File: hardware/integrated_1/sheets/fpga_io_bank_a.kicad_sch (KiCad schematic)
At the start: 1 part, among them U1 XC6SLX9-TQG144

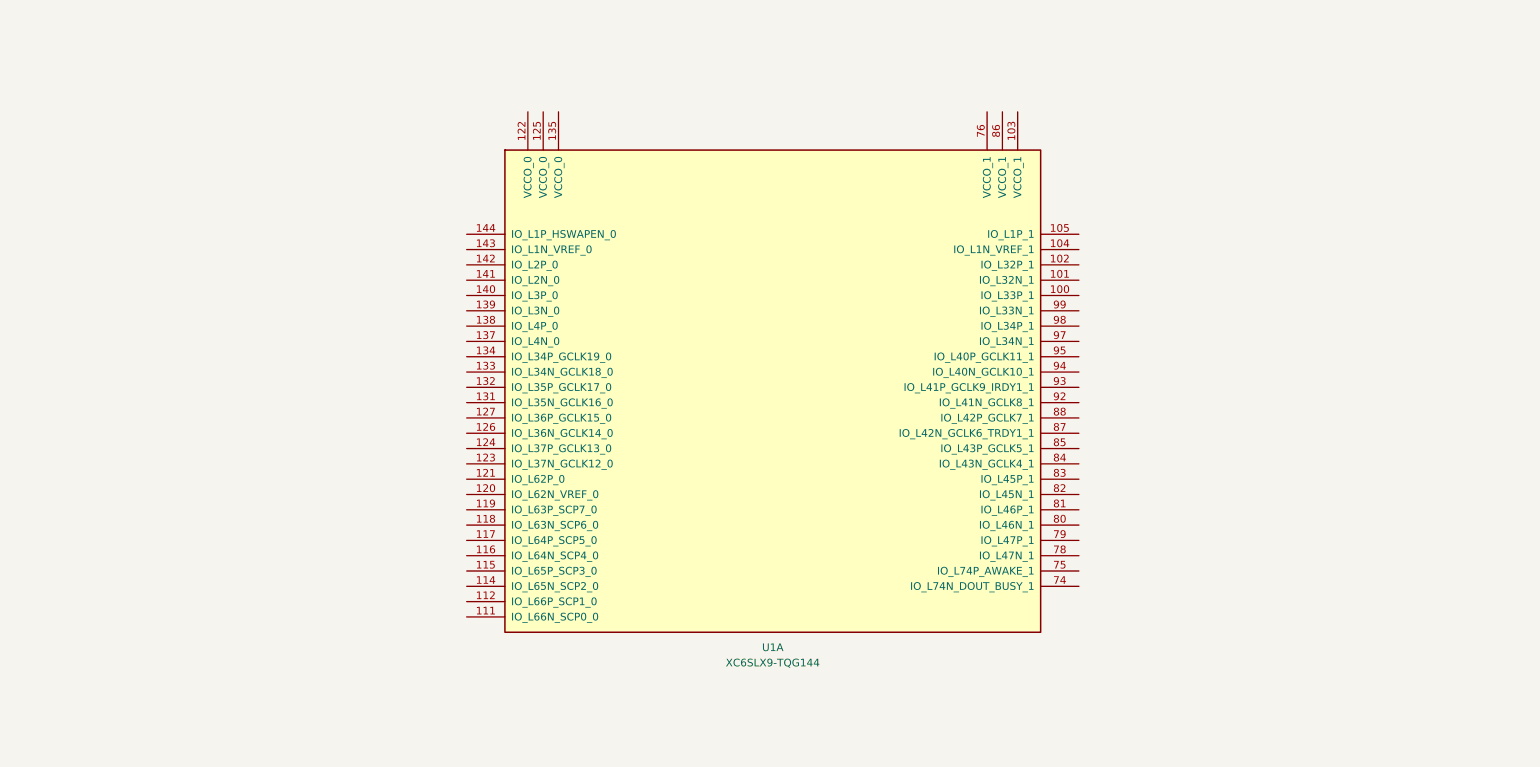
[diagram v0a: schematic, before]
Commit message: hooked up dvi and rp2040 to fpga
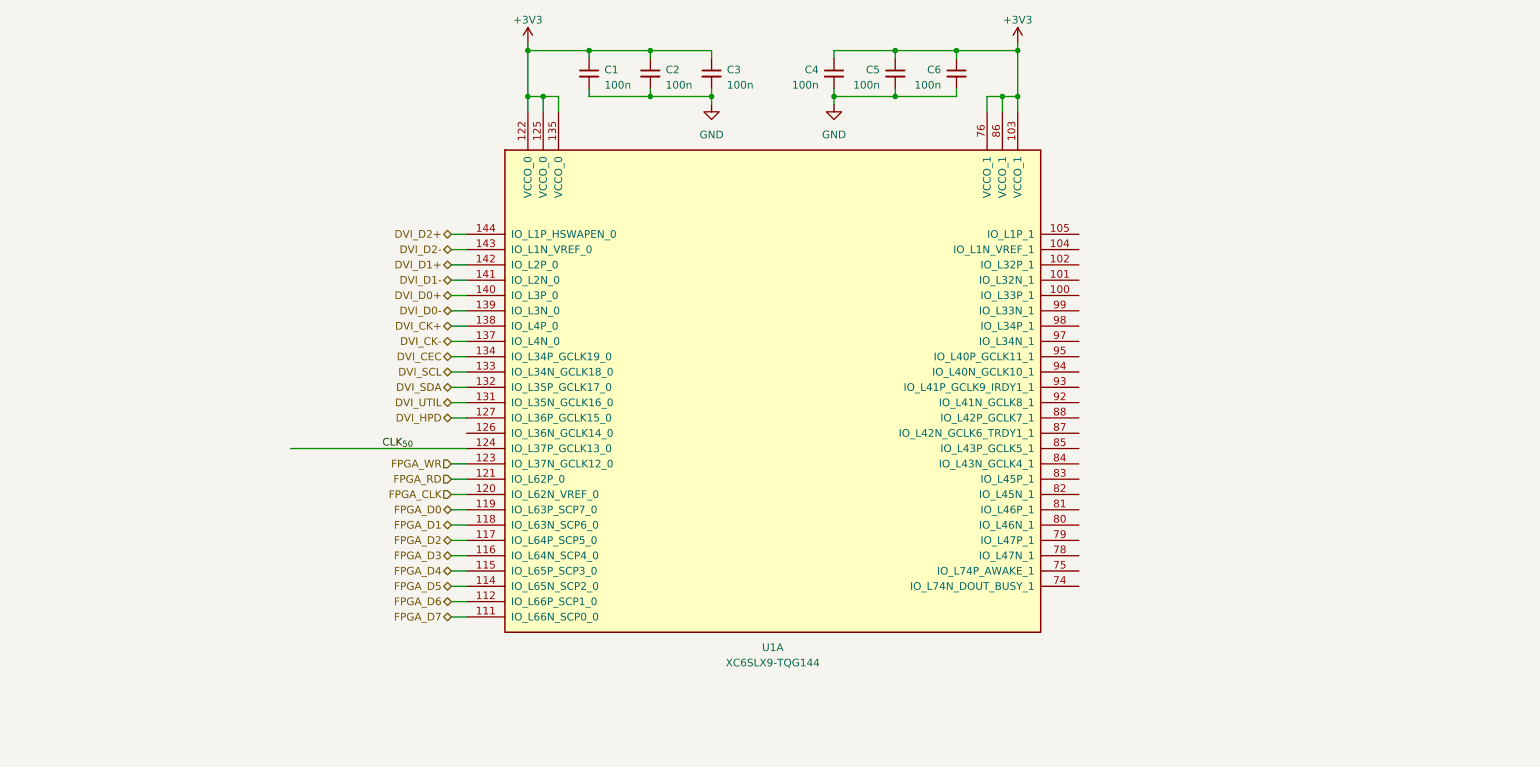
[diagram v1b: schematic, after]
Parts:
- added C1, C2, C3, C4, C5, C6: 100n, Capacitor_SMD:C_0402_1005Metric, symbol Device:C_Small
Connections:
- net +3V3: now reaches U1.103 (VCCO_1)
- net +3V3: now also U1.122 (VCCO_0), U1.125 (VCCO_0), U1.135 (VCCO_0), U1.76 (VCCO_1), U1.86 (VCCO_1), C1.1, C2.1, C3.1, C4.1, C5.1, C6.1
- net FPGA_D7: now reaches U1.111 (IO_L66N_SCP0_0)
- net FPGA_D6: now reaches U1.112 (IO_L66P_SCP1_0)
- net FPGA_D5: now reaches U1.114 (IO_L65N_SCP2_0)
- net FPGA_D4: now reaches U1.115 (IO_L65P_SCP3_0)
- net FPGA_D3: now reaches U1.116 (IO_L64N_SCP4_0)
- net FPGA_D2: now reaches U1.117 (IO_L64P_SCP5_0)
- net FPGA_D1: now reaches U1.118 (IO_L63N_SCP6_0)
- net FPGA_D0: now reaches U1.119 (IO_L63P_SCP7_0)
- net FPGA_CLK: now reaches U1.120 (IO_L62N_VREF_0)
- net FPGA_RD: now reaches U1.121 (IO_L62P_0)
- net FPGA_WR: now reaches U1.123 (IO_L37N_GCLK12_0)
- net CLK_{50}: now reaches U1.124 (IO_L37P_GCLK13_0)
- net DVI_HPD: now reaches U1.127 (IO_L36P_GCLK15_0)
- net DVI_UTIL: now reaches U1.131 (IO_L35N_GCLK16_0)
- net DVI_SDA: now reaches U1.132 (IO_L35P_GCLK17_0)
- net DVI_SCL: now reaches U1.133 (IO_L34N_GCLK18_0)
- net DVI_CEC: now reaches U1.134 (IO_L34P_GCLK19_0)
- net DVI_CK-: now reaches U1.137 (IO_L4N_0)
- net DVI_CK+: now reaches U1.138 (IO_L4P_0)
- net DVI_D0-: now reaches U1.139 (IO_L3N_0)
- net DVI_D0+: now reaches U1.140 (IO_L3P_0)
- net DVI_D1-: now reaches U1.141 (IO_L2N_0)
- net DVI_D1+: now reaches U1.142 (IO_L2P_0)
- net DVI_D2-: now reaches U1.143 (IO_L1N_VREF_0)
- net DVI_D2+: now reaches U1.144 (IO_L1P_HSWAPEN_0)
- new net GND: C1.2, C2.2, C3.2, C4.2, C5.2, C6.2

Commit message: rearranged the pinout to make more sense
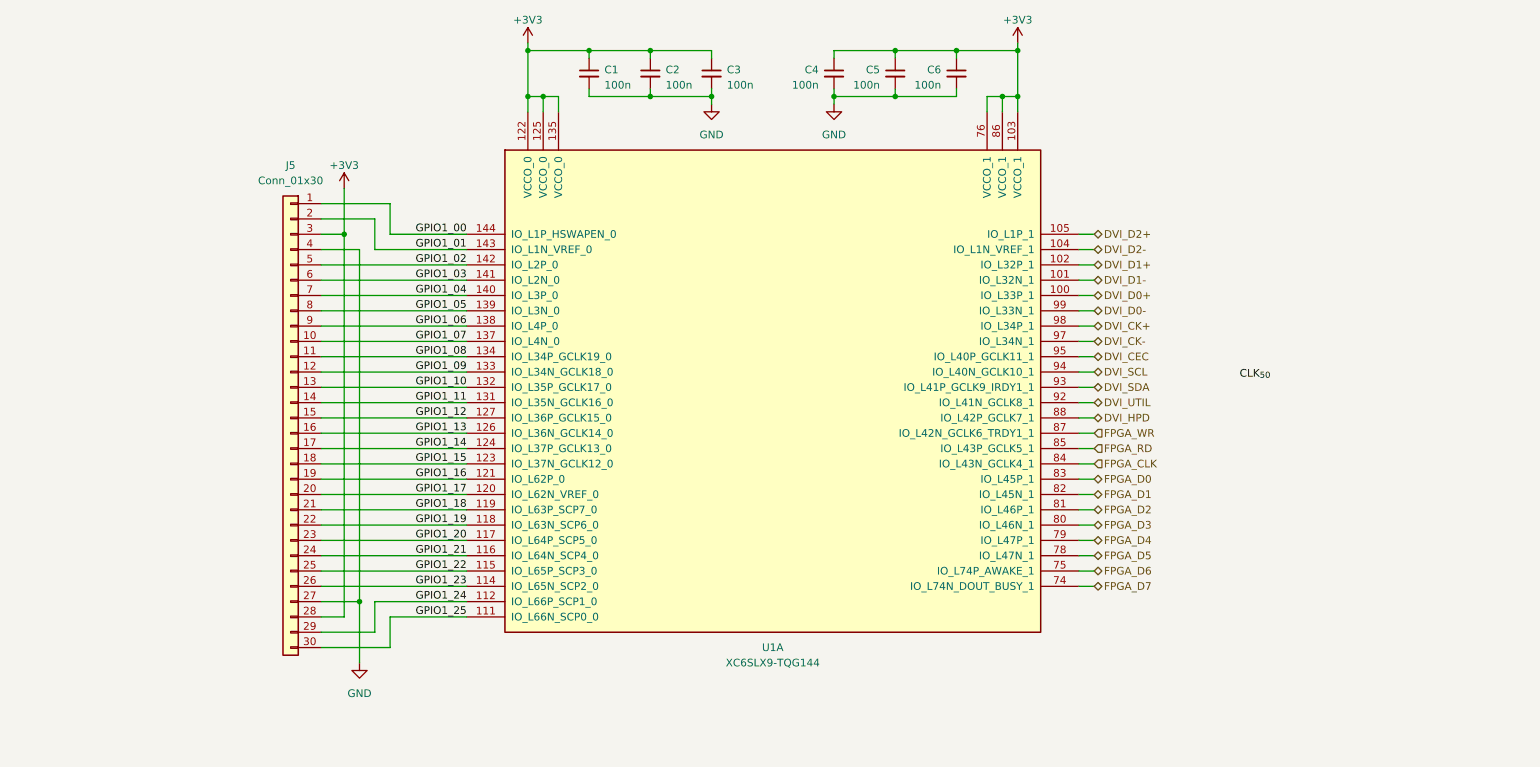
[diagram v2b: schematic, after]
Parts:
- added J5: Conn_01x30, Connector_PinSocket_2.54mm:PinSocket_1x30_P2.54mm_Vertical, symbol Connector_Generic:Conn_01x30
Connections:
- net +3V3: now also J5.28 (Pin_28), J5.3 (Pin_3)
- net CLK_{50}: no longer U1.124 (IO_L37P_GCLK13_0)
- net DVI_CEC: now also U1.95 (IO_L40P_GCLK11_1); no longer U1.134 (IO_L34P_GCLK19_0)
- net DVI_CK+: now also U1.98 (IO_L34P_1); no longer U1.138 (IO_L4P_0)
- net DVI_CK-: now also U1.97 (IO_L34N_1); no longer U1.137 (IO_L4N_0)
- net DVI_D0+: now also U1.100 (IO_L33P_1); no longer U1.140 (IO_L3P_0)
- net DVI_D0-: now also U1.99 (IO_L33N_1); no longer U1.139 (IO_L3N_0)
- net DVI_D1+: now also U1.102 (IO_L32P_1); no longer U1.142 (IO_L2P_0)
- net DVI_D1-: now also U1.101 (IO_L32N_1); no longer U1.141 (IO_L2N_0)
- net DVI_D2+: now also U1.105 (IO_L1P_1); no longer U1.144 (IO_L1P_HSWAPEN_0)
- net DVI_D2-: now also U1.104 (IO_L1N_VREF_1); no longer U1.143 (IO_L1N_VREF_0)
- net DVI_HPD: now also U1.88 (IO_L42P_GCLK7_1); no longer U1.127 (IO_L36P_GCLK15_0)
- net DVI_SCL: now also U1.94 (IO_L40N_GCLK10_1); no longer U1.133 (IO_L34N_GCLK18_0)
- net DVI_SDA: now also U1.93 (IO_L41P_GCLK9_IRDY1_1); no longer U1.132 (IO_L35P_GCLK17_0)
- net DVI_UTIL: now also U1.92 (IO_L41N_GCLK8_1); no longer U1.131 (IO_L35N_GCLK16_0)
- net FPGA_CLK: now also U1.84 (IO_L43N_GCLK4_1); no longer U1.120 (IO_L62N_VREF_0)
- net FPGA_D0: now also U1.83 (IO_L45P_1); no longer U1.119 (IO_L63P_SCP7_0)
- net FPGA_D1: now also U1.82 (IO_L45N_1); no longer U1.118 (IO_L63N_SCP6_0)
- net FPGA_D2: now also U1.81 (IO_L46P_1); no longer U1.117 (IO_L64P_SCP5_0)
- net FPGA_D3: now also U1.80 (IO_L46N_1); no longer U1.116 (IO_L64N_SCP4_0)
- net FPGA_D4: now also U1.79 (IO_L47P_1); no longer U1.115 (IO_L65P_SCP3_0)
- net FPGA_D5: now also U1.78 (IO_L47N_1); no longer U1.114 (IO_L65N_SCP2_0)
- net FPGA_D6: now also U1.75 (IO_L74P_AWAKE_1); no longer U1.112 (IO_L66P_SCP1_0)
- net FPGA_D7: now also U1.74 (IO_L74N_DOUT_BUSY_1); no longer U1.111 (IO_L66N_SCP0_0)
- net FPGA_RD: now also U1.85 (IO_L43P_GCLK5_1); no longer U1.121 (IO_L62P_0)
- net FPGA_WR: now also U1.87 (IO_L42N_GCLK6_TRDY1_1); no longer U1.123 (IO_L37N_GCLK12_0)
- net GND: now also J5.27 (Pin_27), J5.4 (Pin_4)
- net GPIO1_13: now reaches U1.126 (IO_L36N_GCLK14_0)
- net GPIO1_13: now also J5.16 (Pin_16)
- new net GPIO1_00: J5.1 (Pin_1), U1.144 (IO_L1P_HSWAPEN_0)
- new net GPIO1_01: J5.2 (Pin_2), U1.143 (IO_L1N_VREF_0)
- new net GPIO1_02: J5.5 (Pin_5), U1.142 (IO_L2P_0)
- new net GPIO1_03: J5.6 (Pin_6), U1.141 (IO_L2N_0)
- new net GPIO1_04: J5.7 (Pin_7), U1.140 (IO_L3P_0)
- new net GPIO1_05: J5.8 (Pin_8), U1.139 (IO_L3N_0)
- new net GPIO1_06: J5.9 (Pin_9), U1.138 (IO_L4P_0)
- new net GPIO1_07: J5.10 (Pin_10), U1.137 (IO_L4N_0)
- new net GPIO1_08: J5.11 (Pin_11), U1.134 (IO_L34P_GCLK19_0)
- new net GPIO1_09: J5.12 (Pin_12), U1.133 (IO_L34N_GCLK18_0)
- new net GPIO1_10: J5.13 (Pin_13), U1.132 (IO_L35P_GCLK17_0)
- new net GPIO1_11: J5.14 (Pin_14), U1.131 (IO_L35N_GCLK16_0)
- new net GPIO1_12: J5.15 (Pin_15), U1.127 (IO_L36P_GCLK15_0)
- new net GPIO1_14: J5.17 (Pin_17), U1.124 (IO_L37P_GCLK13_0)
- new net GPIO1_15: J5.18 (Pin_18), U1.123 (IO_L37N_GCLK12_0)
- new net GPIO1_16: J5.19 (Pin_19), U1.121 (IO_L62P_0)
- new net GPIO1_17: J5.20 (Pin_20), U1.120 (IO_L62N_VREF_0)
- new net GPIO1_18: J5.21 (Pin_21), U1.119 (IO_L63P_SCP7_0)
- new net GPIO1_19: J5.22 (Pin_22), U1.118 (IO_L63N_SCP6_0)
- new net GPIO1_20: J5.23 (Pin_23), U1.117 (IO_L64P_SCP5_0)
- new net GPIO1_21: J5.24 (Pin_24), U1.116 (IO_L64N_SCP4_0)
- new net GPIO1_22: J5.25 (Pin_25), U1.115 (IO_L65P_SCP3_0)
- new net GPIO1_23: J5.26 (Pin_26), U1.114 (IO_L65N_SCP2_0)
- new net GPIO1_24: J5.29 (Pin_29), U1.112 (IO_L66P_SCP1_0)
- new net GPIO1_25: J5.30 (Pin_30), U1.111 (IO_L66N_SCP0_0)

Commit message: reannotated schematic
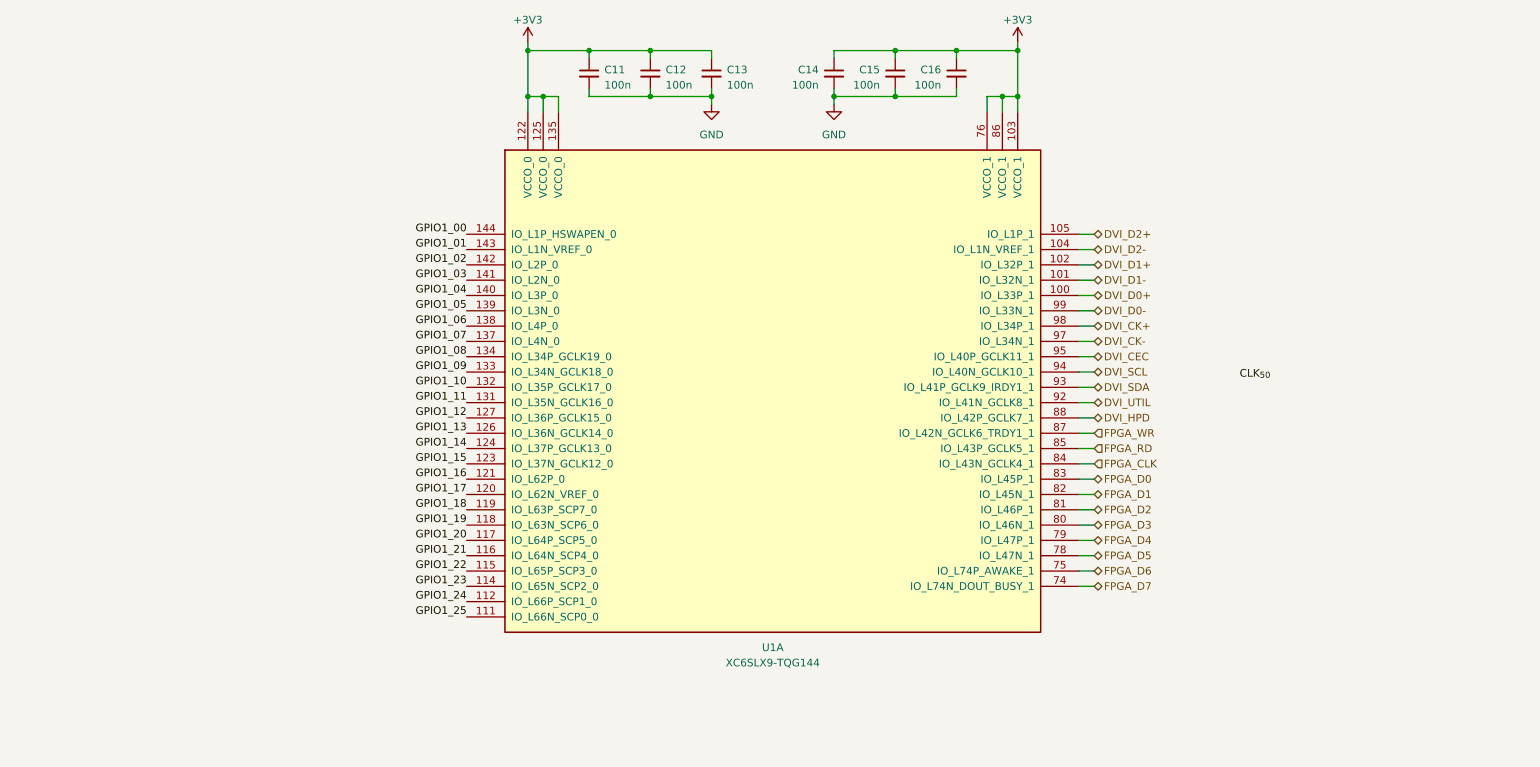
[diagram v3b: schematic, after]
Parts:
- removed J5: Conn_01x30, Connector_PinSocket_2.54mm:PinSocket_1x30_P2.54mm_Vertical, symbol Connector_Generic:Conn_01x30
- C11: renamed from C1; footprint Capacitor_SMD:C_0402_1005Metric -> KiCAD Library:C_0402_1005Metric
- C12: renamed from C2; footprint Capacitor_SMD:C_0402_1005Metric -> KiCAD Library:C_0402_1005Metric
- C13: renamed from C3; footprint Capacitor_SMD:C_0402_1005Metric -> KiCAD Library:C_0402_1005Metric
- C14: renamed from C4; footprint Capacitor_SMD:C_0402_1005Metric -> KiCAD Library:C_0402_1005Metric
- C15: renamed from C5; footprint Capacitor_SMD:C_0402_1005Metric -> KiCAD Library:C_0402_1005Metric
- C16: renamed from C6; footprint Capacitor_SMD:C_0402_1005Metric -> KiCAD Library:C_0402_1005Metric

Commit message: removed gpio references
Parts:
- added JP1, JP2, JP3, JP4: SolderJumper_2_Open, Jumper:SolderJumper-2_P1.3mm_Open_RoundedPad1.0x1.5mm, symbol Jumper:SolderJumper_2_Open
- renumbered C11 to C13, C12 to C14, C13 to C15, C14 to C16, C15 to C17, C16 to C18
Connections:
- net +3V3: now also JP2.1 (A), JP4.1 (A); no longer C13.1, C14.1, C15.1, C16.1, C17.1, C18.1, U1.103 (VCCO_1), U1.122 (VCCO_0), U1.125 (VCCO_0), U1.135 (VCCO_0), U1.76 (VCCO_1), U1.86 (VCCO_1)
- net GPIO1_00: no longer names the net of U1.144 (IO_L1P_HSWAPEN_0)
- net GPIO1_01: no longer names the net of U1.143 (IO_L1N_VREF_0)
- net GPIO1_02: no longer names the net of U1.142 (IO_L2P_0)
- net GPIO1_03: no longer names the net of U1.141 (IO_L2N_0)
- net GPIO1_04: no longer names the net of U1.140 (IO_L3P_0)
- net GPIO1_05: no longer names the net of U1.139 (IO_L3N_0)
- net GPIO1_06: no longer names the net of U1.138 (IO_L4P_0)
- net GPIO1_07: no longer names the net of U1.137 (IO_L4N_0)
- net GPIO1_08: no longer names the net of U1.134 (IO_L34P_GCLK19_0)
- net GPIO1_09: no longer names the net of U1.133 (IO_L34N_GCLK18_0)
- net GPIO1_10: no longer names the net of U1.132 (IO_L35P_GCLK17_0)
- net GPIO1_11: no longer names the net of U1.131 (IO_L35N_GCLK16_0)
- net GPIO1_12: no longer names the net of U1.127 (IO_L36P_GCLK15_0)
- net GPIO1_13: no longer names the net of U1.126 (IO_L36N_GCLK14_0)
- net GPIO1_14: no longer names the net of U1.124 (IO_L37P_GCLK13_0)
- net GPIO1_15: no longer names the net of U1.123 (IO_L37N_GCLK12_0)
- net GPIO1_16: no longer names the net of U1.121 (IO_L62P_0)
- net GPIO1_17: no longer names the net of U1.120 (IO_L62N_VREF_0)
- net GPIO1_18: no longer names the net of U1.119 (IO_L63P_SCP7_0)
- net GPIO1_19: no longer names the net of U1.118 (IO_L63N_SCP6_0)
- net GPIO1_20: no longer names the net of U1.117 (IO_L64P_SCP5_0)
- net GPIO1_21: no longer names the net of U1.116 (IO_L64N_SCP4_0)
- net GPIO1_22: no longer names the net of U1.115 (IO_L65P_SCP3_0)
- net GPIO1_23: no longer names the net of U1.114 (IO_L65N_SCP2_0)
- net GPIO1_24: no longer names the net of U1.112 (IO_L66P_SCP1_0)
- net GPIO1_25: no longer names the net of U1.111 (IO_L66N_SCP0_0)
- new net +2V5: JP1.1 (A), JP3.1 (A)
- new net FPGA_{BANK0}: C13.1, C14.1, C15.1, JP1.2 (B), JP2.2 (B), U1.122 (VCCO_0), U1.125 (VCCO_0), U1.135 (VCCO_0)
- new net FPGA_{BANK1}: C16.1, C17.1, C18.1, JP3.2 (B), JP4.2 (B), U1.103 (VCCO_1), U1.76 (VCCO_1), U1.86 (VCCO_1)
- no-connect marks 0 -> 26
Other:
- moved on the sheet: C13, C14, C15, C16, C17, C18, U1A

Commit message: finalizing the schematic and layout
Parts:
- removed JP1, JP2, JP3, JP4: SolderJumper_2_Open, Jumper:SolderJumper-2_P1.3mm_Open_RoundedPad1.0x1.5mm, symbol Jumper:SolderJumper_2_Open
- added C54: 10n, KiCAD Library:C_0402_1005Metric, symbol Device:C_Small
- added J4: Conn_01x12, Connector_PinHeader_1.00mm:PinHeader_2x06_P1.00mm_Vertical_SMD, symbol Connector_Generic:Conn_01x12
- added U8: XLH335200.000000I, KiCAD Library:XLH335200.000000I, symbol Cuprum:XLH335200.000000I
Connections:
- net FPGA_{BANK0} is gone; now on net +3V3: C13.1, C14.1, C15.1, U1.122 (VCCO_0), U1.125 (VCCO_0), U1.135 (VCCO_0)
- net FPGA_{BANK1} is gone; now on net +3V3: C16.1, C17.1, C18.1, U1.103 (VCCO_1), U1.76 (VCCO_1), U1.86 (VCCO_1)
- net +3V3: now also C54.1, J4.1 (Pin_1), J4.2 (Pin_2), U8.6 (VDD)
- net GND: now also C54.2, J4.3 (Pin_3), J4.4 (Pin_4), U8.3 (GND)
- net PMOD_A7: now reaches U1.111 (IO_L66N_SCP0_0)
- net PMOD_A7: now also J4.12 (Pin_12)
- net PMOD_A6: now reaches U1.112 (IO_L66P_SCP1_0)
- net PMOD_A6: now also J4.11 (Pin_11)
- net PMOD_A5: now reaches U1.114 (IO_L65N_SCP2_0)
- net PMOD_A5: now also J4.10 (Pin_10)
- net PMOD_A4: now reaches U1.115 (IO_L65P_SCP3_0)
- net PMOD_A4: now also J4.9 (Pin_9)
- net PMOD_A3: now reaches U1.116 (IO_L64N_SCP4_0)
- net PMOD_A3: now also J4.8 (Pin_8)
- net PMOD_A2: now reaches U1.117 (IO_L64P_SCP5_0)
- net PMOD_A2: now also J4.7 (Pin_7)
- net PMOD_A1: now reaches U1.118 (IO_L63N_SCP6_0)
- net PMOD_A1: now also J4.6 (Pin_6)
- net PMOD_A0: now reaches U1.119 (IO_L63P_SCP7_0)
- net PMOD_A0: now also J4.5 (Pin_5)
- net CLK_{100N}: now reaches U1.133 (IO_L34N_GCLK18_0)
- net CLK_{100N}: now also U8.5 (O_{2})
- net CLK_{100P}: now reaches U1.134 (IO_L34P_GCLK19_0)
- net CLK_{100P}: now also U8.4 (O_{1})
- no-connect marks 26 -> 18
